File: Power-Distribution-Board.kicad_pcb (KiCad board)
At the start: 2 copper layers, 1 part, among them J1 XT30UPB-F

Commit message: Pressed B
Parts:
- added J10: XT30UPB-F, XT30UPB-F:XT30UPBF, F.Cu at (167.2, 88.7)
- added J11: XT30UPB-F, XT30UPB-F:XT30UPBF, F.Cu at (167.2, 97.0)
- added J12: XT90PB-F, XT90PB-F:XT90PBF, F.Cu at (182.8, 118.0)
- added J2: XT30UPB-F, XT30UPB-F:XT30UPBF, F.Cu at (182.0, 72.2)
- added J3: XT30UPB-F, XT30UPB-F:XT30UPBF, F.Cu at (182.0, 80.5)
- added J4: XT30UPB-F, XT30UPB-F:XT30UPBF, F.Cu at (182.0, 88.8)
- added J5: XT30UPB-F, XT30UPB-F:XT30UPBF, F.Cu at (182.0, 97.0)
- added J6: XT30UPB-F, XT30UPB-F:XT30UPBF, F.Cu at (182.0, 105.5)
- added J7: XT30UPB-F, XT30UPB-F:XT30UPBF, F.Cu at (167.2, 105.5)
- added J8: XT30UPB-F, XT30UPB-F:XT30UPBF, F.Cu at (167.2, 72.0)
- added J9: XT30UPB-F, XT30UPB-F:XT30UPBF, F.Cu at (167.2, 80.3)
- J1: value XT30UPB-F -> XT60PB-F; footprint XT30UPB-F:XT30UPBF -> XT60PB-F:XT60PBF
- moved J1 46.6 mm to (174.2, 61.2), turned to -90 degrees
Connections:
- J1 pad 1: unconnected-(J1-Pad1) -> Net-(J1-+)
- J1 pad 2: unconnected-(J1-Pad2) -> Net-(J1--)
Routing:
- added copper zone on B.Cu, net (none)
- added copper zone on F.Cu, net (none)

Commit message: Circuit "the long way"
how I like my peanut butter jelly
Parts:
- moved J12 84.8 mm to (130.0, 184.5), turned to -90 degrees
- moved J6 74.8 mm to (129.8, 52.0), turned to 180 degrees
- moved J9 74.5 mm to (129.8, 144.8), turned to 180 degrees
- moved J11 71.6 mm to (129.8, 158.0), turned to 180 degrees
- moved J2 62.1 mm to (129.8, 38.5), turned to 180 degrees
- moved J5 61.0 mm to (129.8, 65.5), turned to 180 degrees
- moved J1 59.8 mm to (129.5, 21.5), turned to 180 degrees
- moved J8 59.5 mm to (129.8, 118.2), turned to 180 degrees
- moved J10 56.9 mm to (129.8, 131.5), turned to 180 degrees
- moved J3 53.5 mm to (129.8, 91.8), turned to 180 degrees
- moved J4 53.2 mm to (129.8, 78.8), turned to 180 degrees
- moved J7 37.5 mm to (129.8, 105.0), turned to 180 degrees
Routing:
- removed copper zone on B.Cu, net (none)
- removed copper zone on F.Cu, net (none)

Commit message: Actually properly finally fixed the model
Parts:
- J12: value XT90PB-F -> XT90PB-M; footprint XT90PB-F:XT90PBF -> XT90PB-M:XT90PBM
- moved J12 11.0 mm to (130.0, 173.5), turned to 90 degrees

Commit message: the long way (wholesome)
better PB and J
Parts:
- moved J11 120.3 mm to (133.8, 37.8), turned to 90 degrees
- moved J12 39.8 mm to (131.5, 133.8), turned to -90 degrees
- moved J9 33.2 mm to (133.8, 111.8), turned to 90 degrees
- moved J2 32.5 mm to (133.8, 70.8), turned to 90 degrees
- moved J10 28.3 mm to (133.8, 103.5), turned to 90 degrees
- moved J8 23.1 mm to (133.8, 95.5), turned to 90 degrees
- moved J5 19.9 mm to (133.8, 46.0), turned to 90 degrees
- moved J7 18.2 mm to (133.8, 87.2), turned to 90 degrees
- moved J4 16.7 mm to (133.8, 62.5), turned to 90 degrees
- moved J3 13.4 mm to (133.8, 79.0), turned to 90 degrees
- moved J1 6.66 mm to (131.5, 27.9), turned to 0 degrees
- moved J6 4.59 mm to (133.8, 54.2), turned to 90 degrees

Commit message: stout board
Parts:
- moved J1 102.3 mm to (177.0, 119.5)
- moved J11 89.5 mm to (166.5, 121.0), turned to 0 degrees
- moved J12 87.8 mm to (171.3, 55.5), turned to 180 degrees
- moved J6 68.1 mm to (187.5, 96.0), turned to 0 degrees
- moved J4 57.7 mm to (187.5, 83.5), turned to 0 degrees
- moved J10 56.5 mm to (187.5, 121.0), turned to 0 degrees
- moved J8 55.3 mm to (187.5, 108.5), turned to 0 degrees
- moved J2 53.8 mm to (187.5, 71.0), turned to 0 degrees
- moved J5 49.8 mm to (166.5, 83.5), turned to 0 degrees
- moved J7 33.9 mm to (166.5, 96.0), turned to 0 degrees
- moved J3 33.7 mm to (166.5, 71.0), turned to 0 degrees
- moved J9 32.9 mm to (166.5, 108.5), turned to 0 degrees
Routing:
- added copper zone on F.Cu, net Net-(J1-+)
- added copper zone on B.Cu, net Net-(J1--)

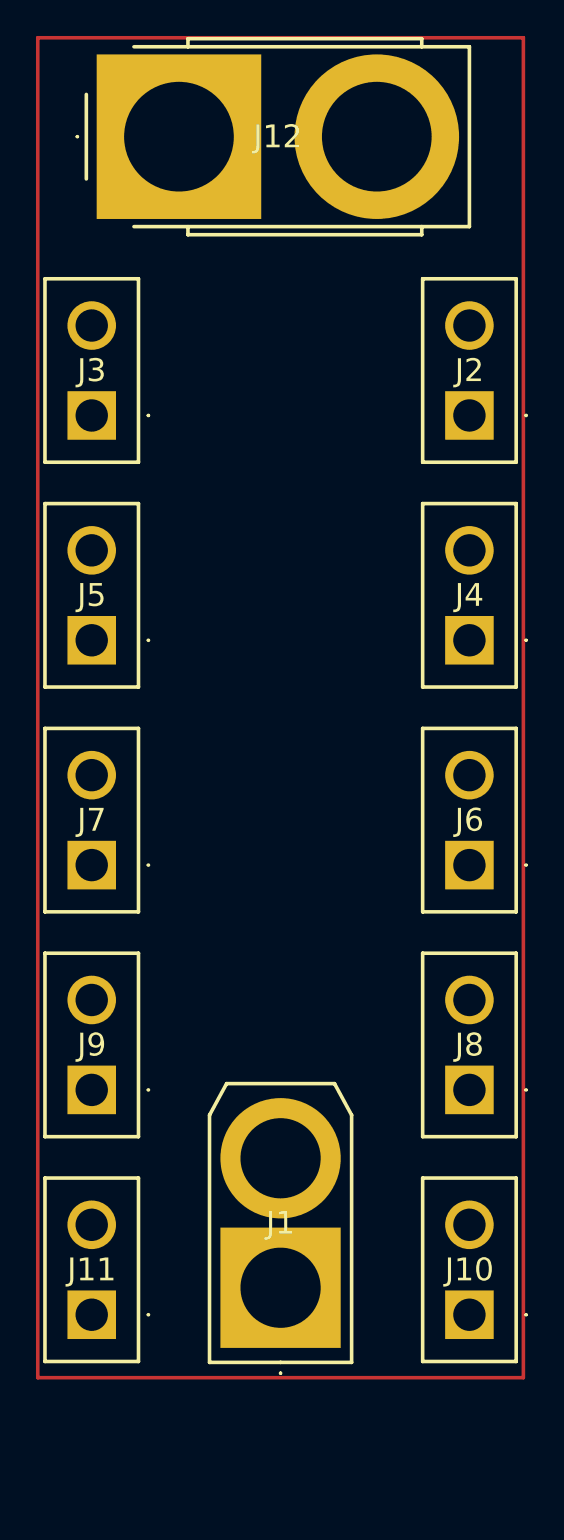
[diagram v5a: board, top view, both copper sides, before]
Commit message: Added screw holes and measurements
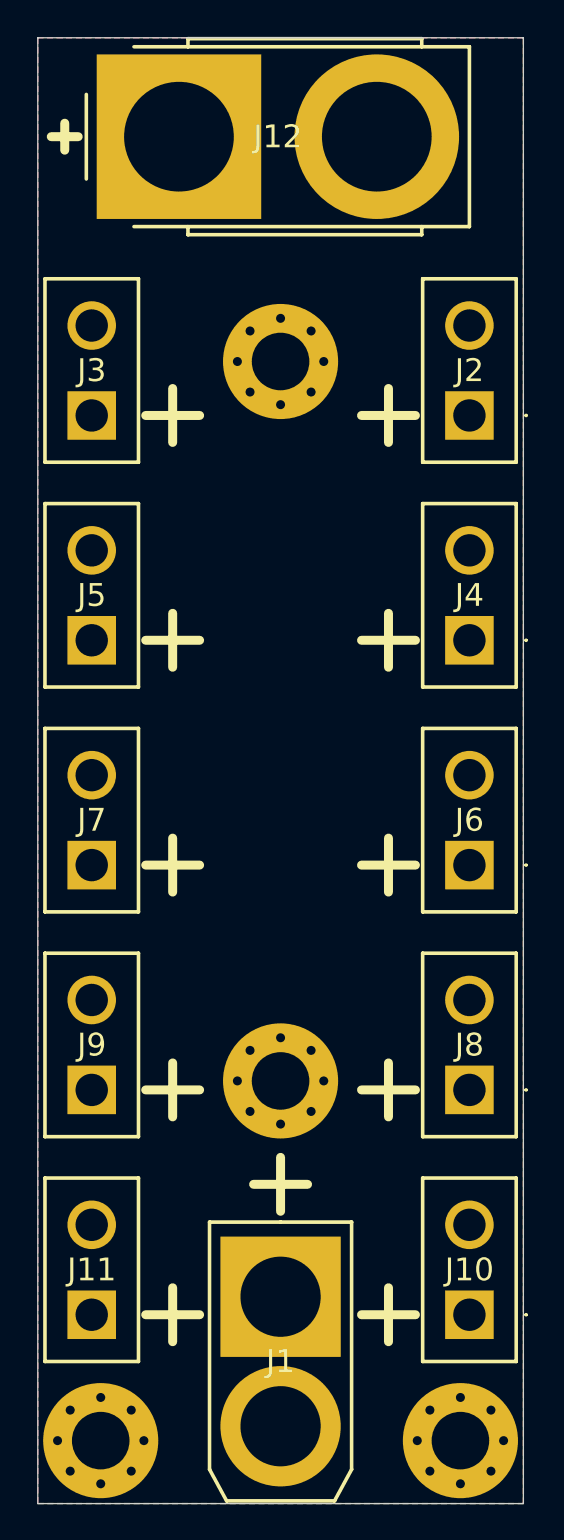
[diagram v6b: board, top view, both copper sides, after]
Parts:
- added REF**: MountingHole_3.2mm_M3_Pad_Via, MountingHole:MountingHole_3.2mm_M3_Pad_Via, F.Cu at (187.0, 128.0)
- added REF**: MountingHole_3.2mm_M3_Pad_Via, MountingHole:MountingHole_3.2mm_M3_Pad_Via, F.Cu at (177.0, 68.0)
- added REF**: MountingHole_3.2mm_M3_Pad_Via, MountingHole:MountingHole_3.2mm_M3_Pad_Via, F.Cu at (167.0, 128.0)
- added REF**: MountingHole_3.2mm_M3_Pad_Via, MountingHole:MountingHole_3.2mm_M3_Pad_Via, F.Cu at (177.0, 108.0)
- moved J1 0.50 mm to (177.0, 120.0), turned to 180 degrees
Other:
- board outline added: 27 x 81.5 mm
